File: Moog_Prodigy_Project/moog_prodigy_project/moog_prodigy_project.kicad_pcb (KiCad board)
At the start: 2 copper layers, 19.8 x 12.9 mm, 303 parts, among them J1 P2-3, J100 NJ2FD-V, J2 P2-4, J3 P2-2, J4 P2-1, J5 P2-1, J6 Conn_01x02_Socket, Q1 CA3046, Q100 CA3046, Q101 CA3046, Q102 BC327, Q103 BC556, Q104 BC550C, Q105 BC550C, Q106 BC550C, Q107 BC550C, Q108 BC550C, Q109 BC550C, Q11 BC107, Q110 BC327, Q111 BC327, Q15 BC549, Q17 BC549, Q2 CA3046, Q4 CA3046, Q6 BC549, SW1 Switch_4x4, SW100 FILTER MODE, SW101 FINAL DECAY SWITCH, SW102 FINAL DECAY SWITCH, SW2 Switch_4x4, SW3 SW_Slide_DPDT_3x3, SW4 Switch_4x4, SW5 Switch_4x4, SW6 Switch_4x4, SW7 SW_Slide_DPDT_3x3, SW8 SW_DPST, SW9 Switch_1x3, T1 230 VAC/ 15VAC 1.5A 22W, U1 NE5532, U10 AD8066ARM, U100 LT1469, U101 LT1228, U102 NE5532, U103 OPA184, U104 OPA184, U105 MC14007UBCP, U106 MC14007UBCP, U107 MC14007UBCP, U12 OPA134, U13 NE5532, U2 NE5532, U2A1 OPA134, U2B1 OPA134, U2B3 OPA134, U3 NE5532, U4 OPA134, U4B1 OPA134, U5 NE5532, U6 LT1011CN8, U67 OPA134, U7 AD8066ARM, U75 L78L12, U76 L79L12, U77 NE556N, U8 NE5532, U9 LT1011CN8

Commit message: problemi sa ca3096, multiplicirani footprintovi
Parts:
- removed the J6 at (27.6, 195.9)
- removed LED1: Led_dioda, LED_THT:LED_D5.0mm
- removed S4-1, S4-2: SW_SPST, L101011ML04Q_1x1:SW_L101011ML04Q
- added J7: Conn_01x02_Socket, Connector_PinSocket_2.54mm:PinSocket_1x02_P2.54mm_Vertical, F.Cu at (365.5, -75.0)
- C20: value 0.01n -> 10p
- R55: renamed from R61; moved to B.Cu
- R63: renamed from R72; value 5.1M -> 5M1
- RV21: renamed from RV107; footprint Potentiometer_THT:Potentiometer_Bourns_3339P_Vertical_HandSoldering -> Potentiometer_THT:Potentiometer_ACP_CA9-V10_Vertical
- SW4: renamed from SW3; footprint CL-SB-22A-02T_3x3:SW_CL-SB-22A-02T -> Button_Switch_THT:SW_CK_JS202011CQN_DPDT_Straight
- SW8: renamed from SW7; footprint CL-SB-22A-02T_3x3:SW_CL-SB-22A-02T -> Button_Switch_THT:SW_CK_JS202011CQN_DPDT_Straight
- U11: renamed from U12; value OPA134 -> OPA234
- U7: renamed from U10; footprint AD8066ARM:SOP65P490X110-8N -> Package_DIP:DIP-8_W7.62mm_Socket
- UI4: footprint MC14007UBDG:SOIC127P600X175-14N -> Package_DIP:DIP-14_W7.62mm_Socket
- moved U13 618.9 mm to (663.6, 184.3), turned to -90 degrees
- moved U14 583.4 mm to (632.2, 161.0), turned to -90 degrees
- moved U10 570.7 mm to (605.0, 175.0), turned to -90 degrees
- moved F1 568.7 mm to (419.3, -207.9), turned to 90 degrees
- moved U12 568.6 mm to (632.9, 192.5), turned to -90 degrees
- moved SW12 556.9 mm to (436.9, -211.9), turned to -90 degrees
- moved T1 547.1 mm to (412.1, -213.9)
- moved U17 540.4 mm to (653.4, 208.5)
- moved D2 521.7 mm to (365.1, -226.7), turned to 180 degrees
- moved CP8 520.3 mm to (371.5, -202.3), turned to 90 degrees
- moved F2 520.0 mm to (391.4, -214.4), turned to -90 degrees
- moved U24 519.5 mm to (355.5, -221.7), turned to -90 degrees
- moved CP7 518.2 mm to (371.5, -219.2), turned to 90 degrees
- moved U25 508.6 mm to (356.0, -201.9), turned to 90 degrees
- moved D1 503.6 mm to (378.9, -213.9)
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- renumbered C2 to C1, C12 to C10, C4 to C11, C3 to C12, C18 to C13, C13 to C14, C16 to C15, C17 to C16, C14 to C17, C15 to C18, C5 to C2, C24 to C21, C21 to C24, C105 to C25, C104 to C26, C106 to C27, C107 to C28, C108 to C29, C6 to C3, C109 to C30, C110 to C31, C111 to C32, C100 to C33, C102 to C34, C101 to C35, C103 to C36, C1 to C4, C7 to C5, C10 to C6, C8 to C7, C9 to C8, C11 to C9, CP102 to CP1, CP106 to CP10, CP104 to CP2, CP108 to CP3, CP109 to CP4, CP105 to CP5, CP103 to CP6, CP100 to CP7, CP107 to CP8, CP101 to CP9, D102 to D1, D101 to D2, D2 to D3, D100 to D4, D103 to D5, J5 to J4, J4 to J5, J100 to J6, Q6 to Q1, Q101 to Q10, Q102 to Q11, Q111 to Q12, Q110 to Q13, Q104 to Q14, Q106 to Q15, Q108 to Q16, Q105 to Q17, Q107 to Q18, Q109 to Q19, Q14 to Q2, Q15 to Q3, Q11 to Q4, Q13 to Q5, Q16 to Q6, Q17 to Q7, Q103 to Q8, Q100 to Q9, R4 to R1, R16 to R10, R110 to R100, R107 to R101, R112 to R102, R113 to R103, R111 to R104, R114 to R105, R115 to R106, R119 to R107, R116 to R108, R108_2 to R108_1, R117 to R109, R17 to R11, R118 to R110, R121 to R111, R120 to R112, R122 to R113, R131 to R114, R138 to R115, R139 to R116, R140 to R117, R137 to R118, R141 to R119, R18 to R12, R142 to R120, R132 to R121, R133 to R122, R134 to R123, R135 to R124, R136 to R125, R125_2 to R125_1, R78 to R126, R126_2 to R126_1, R108 to R127, R127_2 to R127_1, R125 to R128, R128_2 to R128_1, R126 to R129, R9 to R13, R127 to R130, R128 to R131, R130 to R132, R129 to R133, R148 to R134, R143 to R135, R147 to R136, R145 to R137, R149 to R138, R146 to R139, R11 to R14, R144 to R140, R10 to R15, R40 to R16, R41 to R17, R57 to R18, R43 to R19, R5 to R2, R44 to R20, R47 to R21, R48 to R22, R45 to R23, R46 to R24, R49 to R25, R50 to R26, R51 to R27, R52 to R28, R53 to R29, R13 to R3, R55 to R30, R56 to R31, R21 to R32, R22 to R33, R24 to R34, R25 to R35, R26 to R36, R33 to R37, R34 to R38, R36 to R39, R15 to R4, R27 to R40, R19 to R41, R32 to R42, R20 to R43, R31 to R44, R37 to R45, R30 to R46, R38 to R47, R39 to R48, R75 to R49, R12 to R5, R58 to R50, R76 to R51, R63 to R52, R59 to R53, R60 to R54, R65 to R56, R74 to R57, R64 to R58, R73 to R59, R1 to R6, R62 to R60, R66 to R61, R67 to R62, R68 to R64, R70 to R65, R71 to R66, R83 to R67, R84 to R68, R98 to R69, R2 to R7, R100 to R70, R99 to R71, R101 to R72, R102 to R73, R81 to R74, R103 to R75, R170 to R76, R80 to R77, R104 to R78, R6 to R8, R82 to R80, R105 to R81, R29 to R82, R85 to R83, R86 to R84, R89 to R85, R87 to R86, R77 to R87, R95 to R88, R90 to R89, R8 to R9, R91 to R90, R96 to R91, R97 to R93, R93 to R94, R94 to R95, R123 to R96, R124 to R97, R106 to R98, R109 to R99, RV3 to RV1, RV69 to RV10, RV88 to RV11, RV100 to RV12, RV101 to RV13, RV102 to RV14, RV103 to RV15, RV104 to RV16, RV109 to RV17, RV110 to RV18, RV112 to RV19, RV14 to RV2, RV111 to RV20, RV106 to RV22, RV108 to RV23, RV105 to RV24, RV113 to RV25, RV114 to RV26, RV7 to RV3, RV42 to RV4, RV54 to RV5, RV23 to RV6, RV35 to RV7, RV28 to RV8, RV171 to RV9, SW101 to SW10, SW100 to SW11, SW8 to SW12, SW4 to SW2, SW2 to SW3, SW9 to SW6, SW6 to SW7, SW102 to SW9, Q2 to U1, U2 to U10, U67 to U12, U3 to U13, U4 to U14, U100 to U15, U101 to U16, U102 to U17, U104 to U18, U103 to U19, U8 to U2, U77 to U20, U105 to U21, U107 to U22, U106 to U23, U75 to U24, U76 to U25, U2B3 to U2B1, U2B1 to U2B2, U5 to U3, U7 to U4, U6 to U5, U1 to U6, U9 to U8, U13 to U9, UI2 to UI1, Q1 to UI1, Q4 to UI2, UI1 to UI3
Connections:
- net kraj_1 renamed Net-(F1-Pad1)
- net kraj_2 renamed Net-(T1-AB)
- C12 pad 1: Net-(C3-Pad1) -> Net-(C12-Pad1)
- C12 pad 2: Net-(SW2-E) -> Net-(SW3-E)
- R1 pad 2: Net-(R4-Pad2) -> Net-(R1-Pad2)
- R134 pad 2: Net-(R147-Pad1) -> to_VCA/VCF
- R136 pad 1: Net-(R147-Pad1) -> to_VCA/VCF
- R2 pad 1: Net-(R4-Pad2) -> Net-(R1-Pad2)
- R33 pad 2: Net-(R22-Pad2) -> Net-(R33-Pad2)
- R34 pad 2: Net-(R22-Pad2) -> Net-(R33-Pad2)
- R35 pad 1: Net-(R22-Pad2) -> Net-(R33-Pad2)
- R36 pad 1: Net-(R22-Pad2) -> Net-(R33-Pad2)
- R40 pad 2: Net-(R27-Pad2) -> Net-(R40-Pad2)
- R42 pad 2: Net-(Q1-Pad10) -> Net-(R42-Pad2)
- R43 pad 2: Net-(SW2-E) -> Net-(SW3-E)
- R44 pad 2: Net-(Q1-Pad10) -> Net-(R42-Pad2)
- R48 pad 2: Net-(Q1-Pad7) -> Net-(R48-Pad2)
- R5 pad 2: Net-(U2B3-+) -> Net-(U2B1-+)
- R51 pad 1: Net-(S4-2-B) -> /Left_side_pt2/ANODA
- R52 pad 3: Net-(R63-Pad3) -> Net-(R52-Pad3)
- R76 pad 2: Right side schematic bottom flag to R145 100K -> to_VCA/VCF
- R8 pad 2: Net-(R6-Pad2) -> Net-(R8-Pad2)
- R82 pad 2: SW8 PREKIDAC KOD BABICA FILTER MODE -> OSC_MOD_SWITCH
- R9 pad 2: Net-(R8-Pad2) -> Net-(R9-Pad2)
- R94 pad 2: Pocetak_Babicevog_dela_Leader -> enter_CP102
- R95 pad 1: Pocetak_Babicevog_dela_Leader -> enter_CP102
- RV3 pad 3: Net-(R6-Pad2) -> Net-(R8-Pad2)
- RV4 pad 2: Net-(RV42-Pad2) -> Net-(RV4-Pad2)
- RV4 pad 3: Net-(RV42-Pad2) -> Net-(RV4-Pad2)
- RV8 pad 3: Net-(R27-Pad2) -> Net-(R40-Pad2)
- SW12 pad 2: Net-(J6-Pin_1) -> /voltage_source/N
- SW12 pad 4: Net-(J6-Pin_2) -> /voltage_source/L
- SW3 pad 5: Net-(SW2-E) -> Net-(SW3-E)
- SW7 pad 4: Flag na  R118 ulaz na donji deo desne polovine -> FILTER_KYBD_CONTROL
- SW8 pad 2: SW8 PREKIDAC KOD BABICA FILTER MODE -> OSC_MOD_SWITCH
- U1 pad 12: Net-(U4B1-+) -> (no net)
- U1 pad 13: GND -> (no net)
- U1 pad 14: unconnected-(Q2-Pad14) -> (no net)
- U1 pad 6: (no net) -> GND
- U1 pad 7: (no net) -> Net-(R48-Pad2)
- U1 pad 8: (no net) -> +12V
- U2B1 pad 3: Net-(U2B3-+) -> Net-(U2B1-+)
- U2B2 pad 2: Net-(SW2-E) -> Net-(SW3-E)
- U2B2 pad 6: Net-(C3-Pad1) -> Net-(C12-Pad1)
- U4 pad 3: Net-(RV42-Pad2) -> Net-(RV4-Pad2)
- U7 pad 3: Net-(R63-Pad3) -> Net-(R52-Pad3)
- UI1 pad 1: Net-(RV42-Pad2) -> Net-(RV4-Pad2)
- UI1 pad 10: (no net) -> Net-(R42-Pad2)
- UI1 pad 11: (no net) -> unconnected-(UI1-Pad11)
- UI1 pad 12: (no net) -> Net-(U2B1-+)
- UI1 pad 13: (no net) -> GND
- UI1 pad 14: (no net) -> unconnected-(UI1-Pad14)
- UI1 pad 2: Net-(R4-Pad2) -> Net-(R1-Pad2)
- UI1 pad 3: Net-(R8-Pad2) -> Net-(R9-Pad2)
- UI1 pad 4: Net-(R6-Pad2) -> Net-(R8-Pad2)
- UI1 pad 9: (no net) -> unconnected-(UI1-Pad9)
- UI1 pad 1: (no net) -> Net-(RV4-Pad2)
- UI1 pad 10: Net-(Q1-Pad10) -> Net-(R42-Pad2)
- UI1 pad 11: unconnected-(Q1-Pad11) -> unconnected-(UI1-Pad11)
- UI1 pad 12: Net-(U2B3-+) -> Net-(U2B1-+)
- UI1 pad 14: unconnected-(Q1-Pad14) -> unconnected-(UI1-Pad14)
- UI1 pad 2: (no net) -> Net-(R1-Pad2)
- UI1 pad 3: (no net) -> Net-(R9-Pad2)
- UI1 pad 4: (no net) -> Net-(R8-Pad2)
- UI1 pad 5: (no net) -> Net-(SW1-E)
- UI1 pad 6: GND -> (no net)
- UI1 pad 7: Net-(Q1-Pad7) -> (no net)
- UI1 pad 8: +12V -> (no net)
- UI1 pad 9: unconnected-(Q1-Pad9) -> unconnected-(UI1-Pad9)
- UI2 pad 1: (no net) -> Net-(R52-Pad3)
- UI2 pad 12: (no net) -> Net-(U4B1-+)
- UI2 pad 13: (no net) -> GND
- UI2 pad 14: (no net) -> unconnected-(UI2-Pad14)
- UI2 pad 2: (no net) -> Net-(R33-Pad2)
- UI2 pad 3: (no net) -> Net-(C12-Pad1)
- UI2 pad 4: (no net) -> Net-(R40-Pad2)
- UI2 pad 5: (no net) -> Net-(SW3-E)
- UI4 pad 3: Right side schematic bottom flag to R145 100K -> to_VCA/VCF
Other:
- board size 19.8 x 12.9 mm -> 12.9 x 19.8 mm

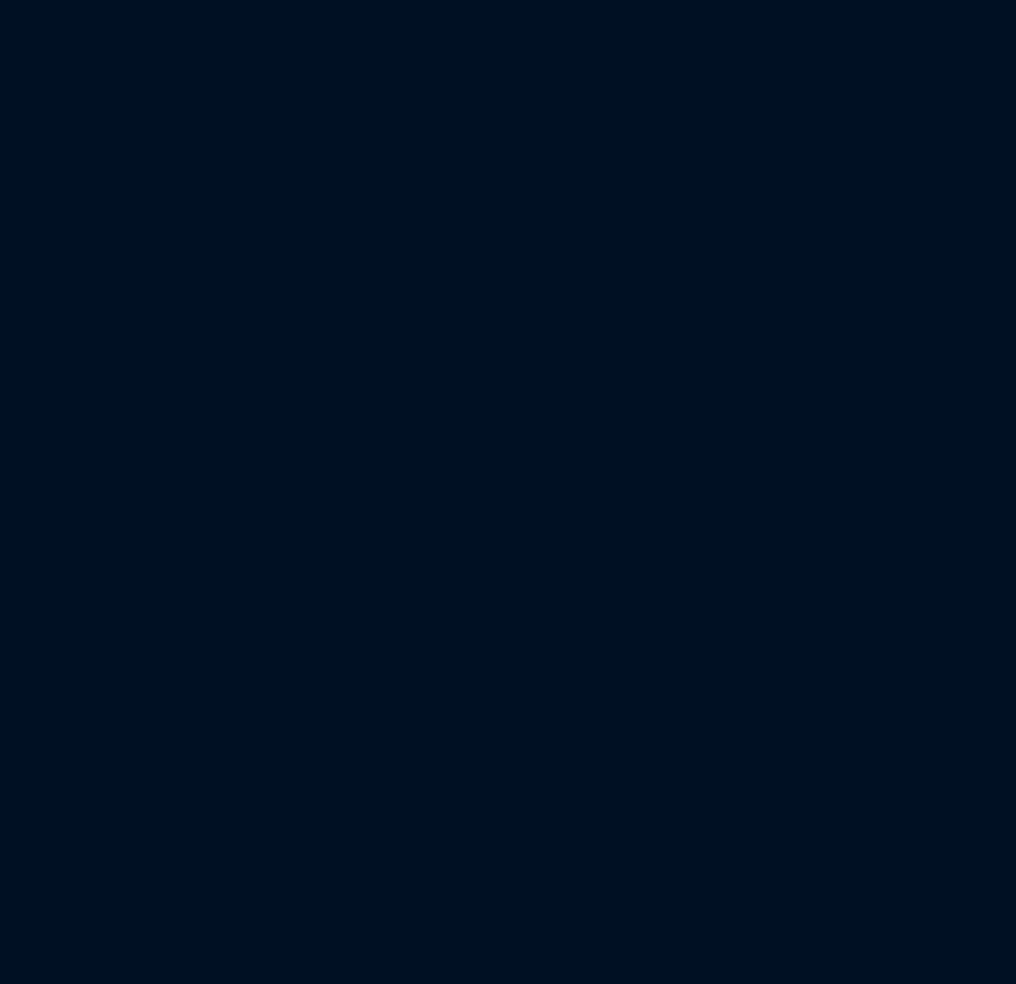
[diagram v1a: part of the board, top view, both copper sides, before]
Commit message: CA3046 leva strana seme update
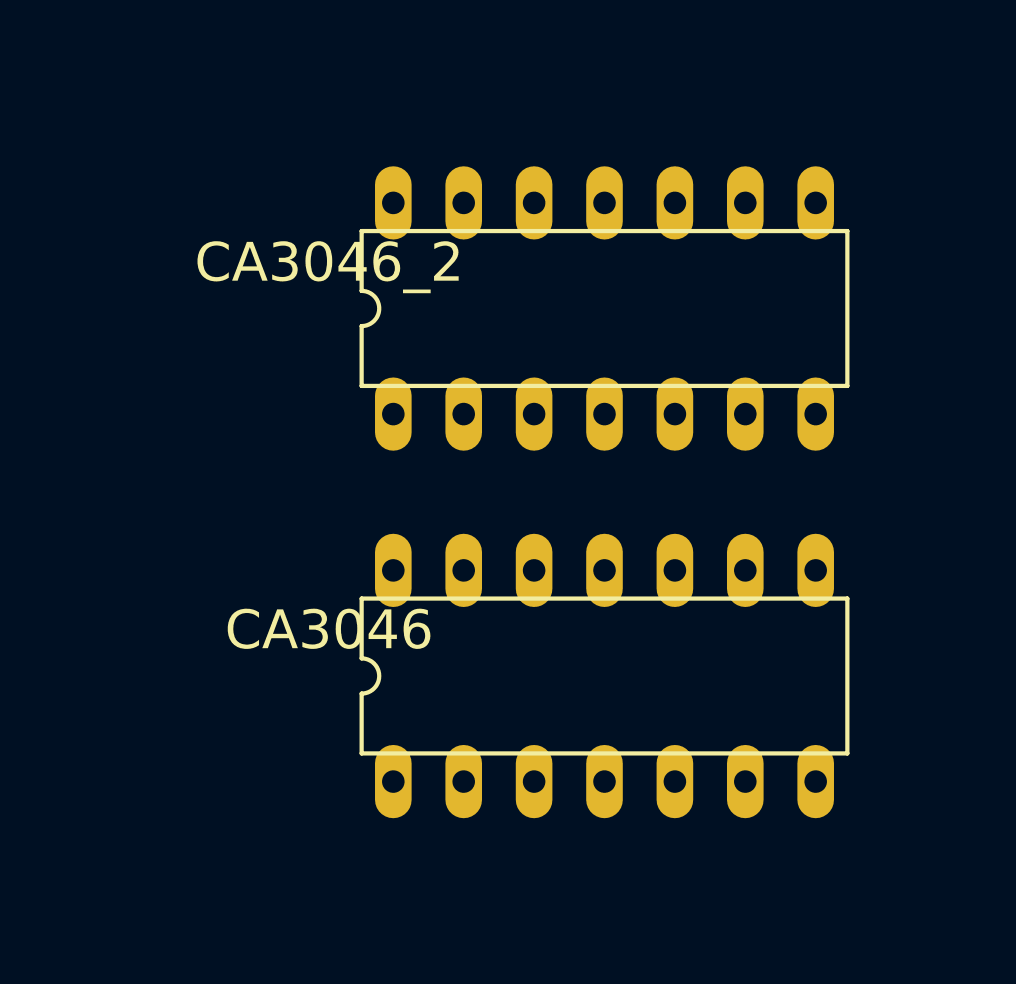
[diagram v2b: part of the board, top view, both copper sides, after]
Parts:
- added CA3046: CA3046, CA3046:DIL14, F.Cu at (627.4, 57.8)
- added CA3046_2: CA3046_2, CA3046:DIL14, F.Cu at (627.4, 44.5)
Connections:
- R1 pad 2: Net-(R1-Pad2) -> Net-(CA3046-Pad2)
- R12 pad 2: Net-(R12-Pad2) -> Net-(CA3046-Pad7)
- R14 pad 2: Net-(R14-Pad2) -> Net-(CA3046-Pad13)
- R15 pad 2: Net-(R14-Pad2) -> Net-(CA3046-Pad13)
- R2 pad 1: Net-(R1-Pad2) -> Net-(CA3046-Pad2)
- R33 pad 2: Net-(R33-Pad2) -> Net-(CA3046_2-Pad2)
- R34 pad 2: Net-(R33-Pad2) -> Net-(CA3046_2-Pad2)
- R35 pad 1: Net-(R33-Pad2) -> Net-(CA3046_2-Pad2)
- R36 pad 1: Net-(R33-Pad2) -> Net-(CA3046_2-Pad2)
- R40 pad 2: Net-(R40-Pad2) -> Net-(CA3046_2-Pad4)
- R42 pad 2: Net-(R42-Pad2) -> Net-(CA3046_2-Pad13)
- R44 pad 2: Net-(R42-Pad2) -> Net-(CA3046_2-Pad13)
- R48 pad 2: Net-(R48-Pad2) -> Net-(CA3046_2-Pad7)
- R52 pad 3: Net-(R52-Pad3) -> Net-(CA3046_2-Pad1)
- R8 pad 2: Net-(R8-Pad2) -> Net-(CA3046-Pad4)
- R9 pad 2: Net-(R9-Pad2) -> Net-(CA3046-Pad3)
- RV3 pad 3: Net-(R8-Pad2) -> Net-(CA3046-Pad4)
- RV4 pad 2: Net-(RV4-Pad2) -> Net-(CA3046-Pad1)
- RV4 pad 3: Net-(RV4-Pad2) -> Net-(CA3046-Pad1)
- RV8 pad 3: Net-(R40-Pad2) -> Net-(CA3046_2-Pad4)
- U4 pad 3: Net-(RV4-Pad2) -> Net-(CA3046-Pad1)
- U7 pad 3: Net-(R52-Pad3) -> Net-(CA3046_2-Pad1)

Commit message: Left side PCB update final
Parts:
- removed U1, UI1 (x2), UI2: CA3046, CA3046:DIL14
- moved CA3046 587.2 mm to (40.2, 50.0)
- moved CA3046_2 580.7 mm to (48.7, 93.1)
- moved RV6 420.6 mm to (20.4, 106.9)
- moved R32 420.6 mm to (28.4, 106.9)
- moved R40 413.2 mm to (41.7, 113.8), turned to 0 degrees
- moved R33 405.1 mm to (43.4, 107.9), turned to 90 degrees
- moved U2B2 400.3 mm to (33.4, 117.4), turned to 180 degrees
- moved C12 399.4 mm to (23.4, 115.9)
- moved R36 396.2 mm to (48.7, 100.2), turned to -90 degrees
- moved R34 391.8 mm to (36.4, 89.5)
- moved R35 390.4 mm to (53.4, 100.2)
- moved RV8 371.5 mm to (57.4, 116.4)
- moved R52 367.5 mm to (87.9, 93.1)
- moved R46 353.8 mm to (64.7, 108.8), turned to -90 degrees
- moved R38 342.9 mm to (69.4, 116.2)
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
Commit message: SMD component to THT component update PCB
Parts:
- U4: value AD8066ARM -> NE5532; footprint AD8066ARM:SOP65P490X110-8N -> NE5532AP:DIP794W45P254L1016H508Q8
- U7: value AD8066ARM -> NE5532; footprint Package_DIP:DIP-8_W7.62mm_Socket -> NE5532AP:DIP794W45P254L1016H508Q8
- moved U4 89.6 mm to (36.0, 35.0), turned to -90 degrees
- moved RV6 19.2 mm to (23.0, 87.9), turned to 180 degrees
- moved C12 15.5 mm to (38.5, 119.4), turned to 90 degrees
- moved J4 12.6 mm to (164.5, 43.0)
- moved U7 11.1 mm to (68.5, 61.4)
- moved R2 10.7 mm to (15.7, 52.4), turned to 0 degrees
- moved J5 9.26 mm to (182.0, 43.0)
- moved RV9 9.01 mm to (103.5, 95.0)
- moved R72 8.73 mm to (187.9, 84.1)
- moved R89 8.73 mm to (187.9, 68.1)
- moved R93 8.73 mm to (187.9, 78.1)
- moved U2 8.73 mm to (219.2, 98.0)
- moved R69 8.73 mm to (168.0, 87.3)
- moved R79 8.73 mm to (224.5, 68.6)
- moved R82 8.73 mm to (157.5, 88.6)
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
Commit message: raspored i edge cut
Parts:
- removed U10, U13: NE5532, NE5532AP:DIP794W45P254L1016H508Q8
- removed U12, U14: OPA134, OPA134PA:DIP794W45P254L959H508Q8
- removed U17: NE5532, Package_DIP:DIP-8_W7.62mm
- removed the UI3 at (148.3, -178.2)
- moved D2 540.2 mm to (162.9, 149.3)
- moved D3 540.2 mm to (151.7, 166.8)
- moved C33 540.2 mm to (161.3, 156.9)
- moved C34 540.2 mm to (160.8, 173.8)
- moved C35 540.2 mm to (146.8, 154.4)
- moved C36 540.2 mm to (146.3, 171.6)
- moved CP7 540.2 mm to (169.3, 156.9)
- moved CP8 540.2 mm to (169.3, 173.8)
- moved CP9 540.2 mm to (130.3, 154.7)
- moved D1 540.2 mm to (176.7, 162.1)
- moved D4 540.2 mm to (138.8, 150.9)
- moved D5 540.2 mm to (138.8, 167.5)
- moved F2 540.2 mm to (189.2, 161.6)
- moved U24 540.2 mm to (153.3, 154.3)
- moved U25 540.2 mm to (153.8, 174.1)
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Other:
- board size 12.9 x 19.8 mm -> 288.5 x 178.5 mm
